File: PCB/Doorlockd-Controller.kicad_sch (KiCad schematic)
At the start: 58 parts, among them J10 Power Out 1, J11 Audio out, J12 GPIO 3, J13 Debug UART, J14 GPIO 4, J15 Power Out 2, J16 to extra screw conn., J18 GPIO only MilkV 1.8V, J19 3V 5V Vin, J20 3V 5V Vin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

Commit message: Added kibot workflow for automatic versioning
see https://github.com/matthijskooijman/PCB-workflows
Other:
- title: Doorlockd - BBB PCB -> Doorlockd-Controller (Rock pi-S/Milk-V duo S)
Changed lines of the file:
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@@
 	(paper "A4")
 	(title_block
-		(title "Doorlockd - BBB PCB")
-		(date "2019-06-11")
-		(rev "v0.02")
+		(title "Doorlockd-Controller (Rock pi-S/Milk-V duo S)")
+		(date "2025-06-17")
+		(rev "v2.0")
 		(comment 1 "author: Diederik Hamelink")
 		(comment 2 "CC BY 4.0")
+		(comment 3 "github.com/doorlockd")
 		(comment 4 "de WAR")
 	)
@@
 			"AAcAAAAHAAAABwAAAAcAAAAHAAAABwAAAAcAAAAHAAAABwAAAAcAAAAHAAAABwAAAAcAAAAHAAAA"
 			"BwAAAAcAAAAHAAAABwAAAAcAAAAHAAAABwAAAAcAAAAHAAAABwAAAAcAAAAHAAAABwAAAAcAAAAH"
-			"AAAABwAAAA=="
+			"AAAABwAAAAABAAAA8M3TJgEAAAAIBwAAAQAAAJDN0yYBAAAAEQAAAAEAAABgy9MmAQAAAODN0yYB"
+			"AAAAAAAAAAAAAAD/AQAAFgAAAP8BAABFAAAAGAAAAAEAAACwtbUHAQAAAAEAAAABAAAATQcAABMA"
+			"AAD/AQAAFgAAAP8BAAAgAAAATQQAAAEAAABAztMmAQAAAAkHAAABAAAAQMvTJgEAAABLBAAAIgAA"
+			"AEDO0yYBAAAACQcAAAEAAACgztMmAQAAADgEAAABAAAAQM7TJgEAAAAJBwAAIgAAAMDO0yYBAAAA"
+			"NwQAAAEAAABAztMmAQAAAAkHAAAAAAAA4M7TJgEAAAA2BAAAFwAAAEDO0yYBAAAACQcAAAEAAAAA"
+			"z9MmAQAAACoEAAABAAAAQM7TJgEAAAAJBwAAAQAAACDP0yYBAAAADwAAAAEAAABAztMmAQAAAAAA"
+			"AAAAAAAAYSIAAAEAAABIz9MmAQAAADcEAAABAAAAyM7TJgEAAAD/AQAAEAAAAP8BAABFAAAA8gMA"
+			"ACcAAABgz9MmAQAAAAkHAAABAAAAYMrTJgEAAAABAAAAAAAAAGDP0yYBAAAAcwQAADUAAAAAAAAA"
+			"AAAAAAoHAAABAAAAAAAAAAAAAABsBAAAAQAAAAAAAAAAAAAA/wAAAAEBAAAAgrwmAQAAAPAPUwAA"
+			"YAAAwA9TAABgAACAEFMAAGAAAAARUwAAYAAAABJTAABgAAAAAAAAAAAAAAAAAAAAAAAAAAAAAAAA"
+			"AAAAAAAAAAAAAAAAAAAAAAAAAAAAAAAAAAAAAAAAAAAAAAAAAAAAYAAAAAAAAAAAAAAAAAAAAAAA"
+			"AAAAAAAAAAAAAgAAAAAAAAAAAAAAAAAAAAAIbQYAYAAA4CvJAwBgAAAjAAAAAAAAACgAAAAAAACA"
+			"gB9TAABgAABAIFMAAGAAAAAhUwAAYAAAwCFTAABgAACAIlMAAGAAAEAjUwAAYAAAACRTAABgAADA"
+			"JFMAAGAAAIAlUwAAYAAAQCZTAABgAAAAJ1MAAGAAAPAzkWMBAAAAIDaRYwEAAABQOJFjAQAAAIA6"
+			"kWMBAAAAsDyRYwEAAADgPpFjAQAAABBBkWMBAAAAQEORYwEAAABwRZFjAQAAAKBHkWMBAAAA0EmR"
+			"YwEAAADAJ1MAAGAAAIAoUwAAYAAAQClTAABgAAAAKlMAAGAAAMAqUwAAYAAAgCtTAABgAABALFMA"
+			"AGAAAAAtUwAAYAAAwC1TAABgAACALlMAAGAAAEAvUwAAYAAAADBTAABgAADAMFMAAGAAAIAxUwAA"
+			"YAAAQDJTAABgAAAAM1MAAGAAAMAzUwAAYAAAgDRTAABgAABANVMAAGAAAAA2UwAAYAAAwDZTAABg"
+			"AACAN1MAAA=="
 		)
 	)

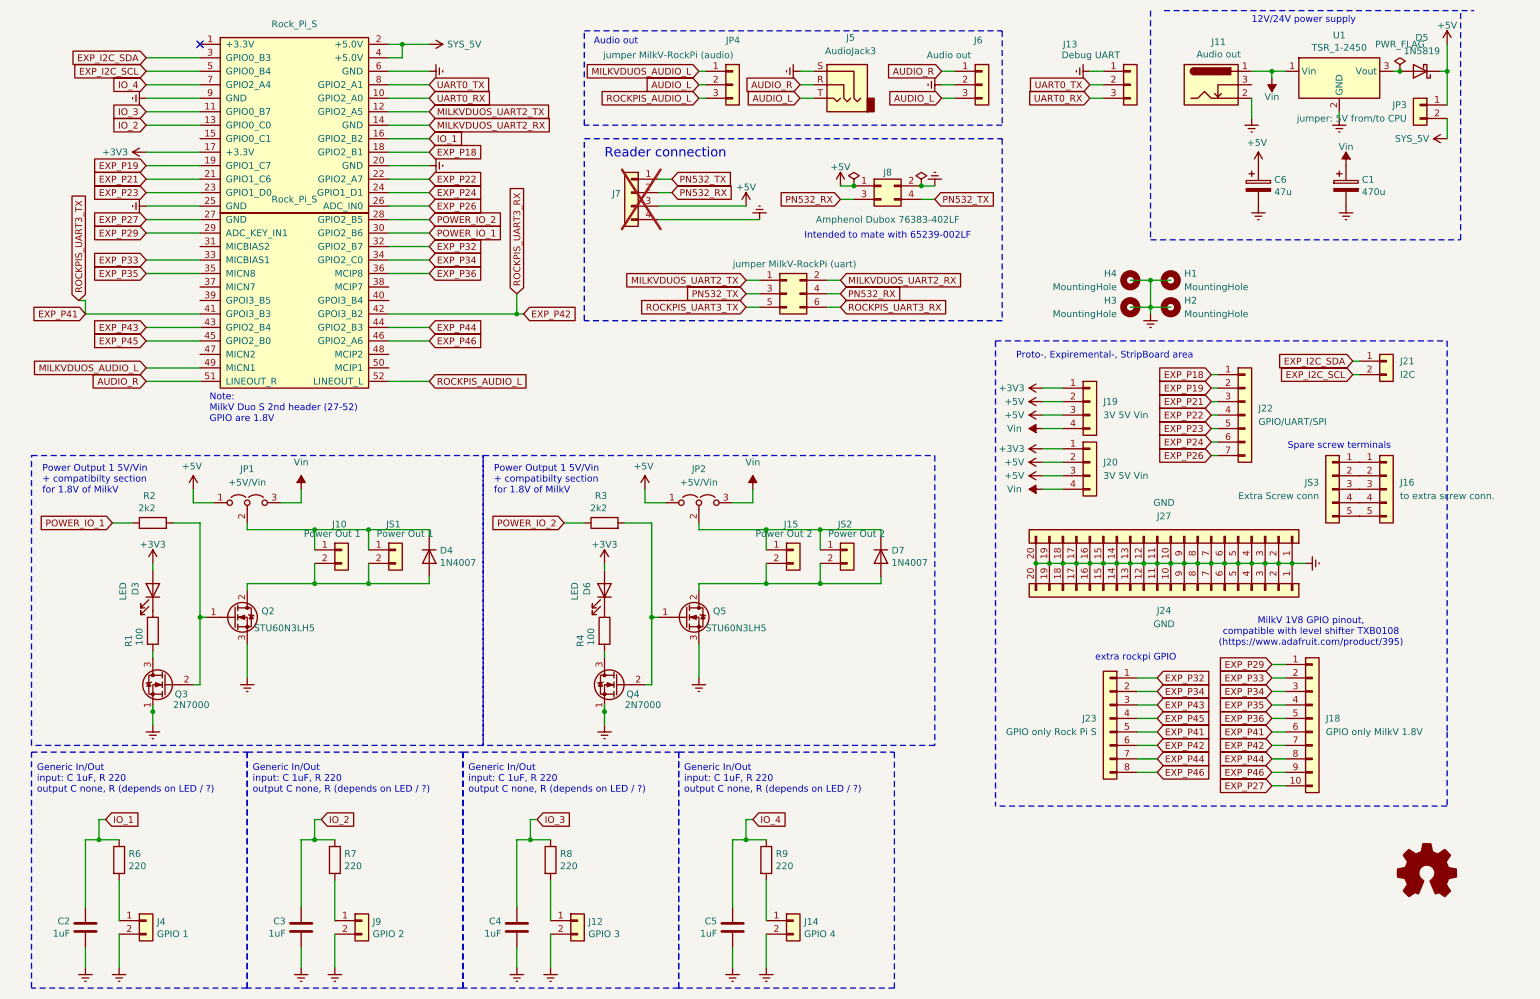
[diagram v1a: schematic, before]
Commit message: Fixed various ERC rule errors and warnings
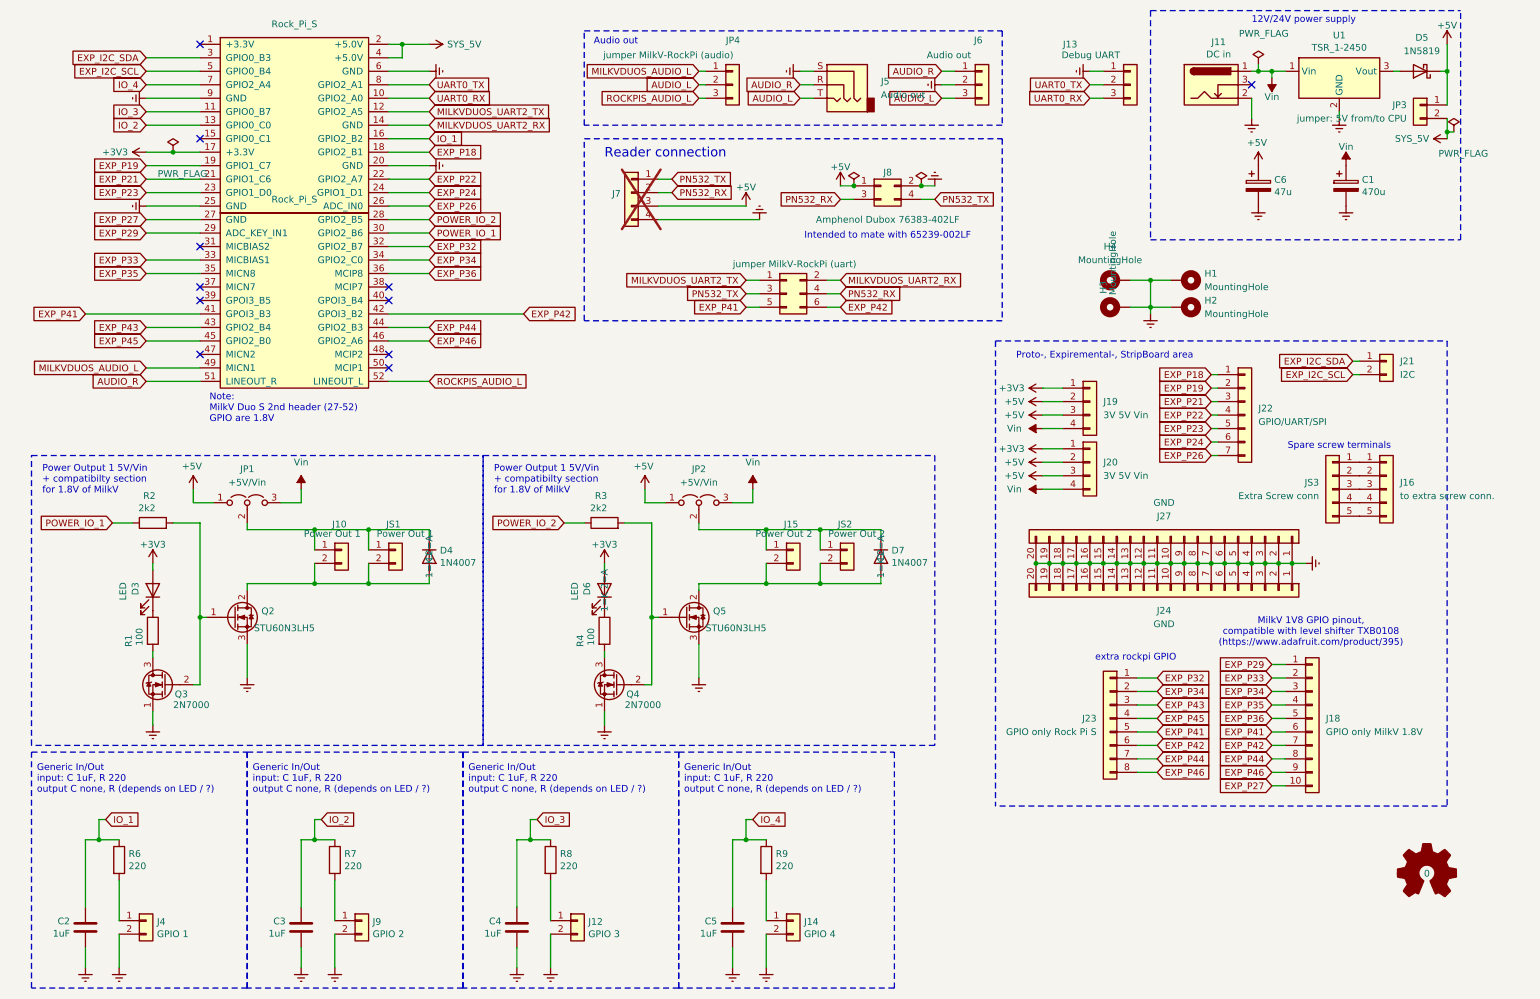
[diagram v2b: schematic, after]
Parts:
- D4, D7: footprint Diode_THT:D_DO-41_SOD81_P7.62mm_Horizontal -> Diode_THT:D_DO-41_SOD81_P10.16mm_Horizontal
- H1, H2, H3, H4: symbol Mechanical:MountingHole -> Mechanical:MountingHole_Pad
- J11: value Audio out -> DC in
- J5: value AudioJack3 -> Audio out
- Q2, Q5: symbol Device:Q_NMOS_GDS -> Transistor_FET:Q_NMOS_GDS
- Q3, Q4: footprint Package_TO_SOT_THT:TO-92_Wide -> Package_TO_SOT_THT:TO-92_Inline
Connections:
- net Earth: now also H1.1, H2.1, H3.1, H4.1
- no-connect marks 1 -> 11

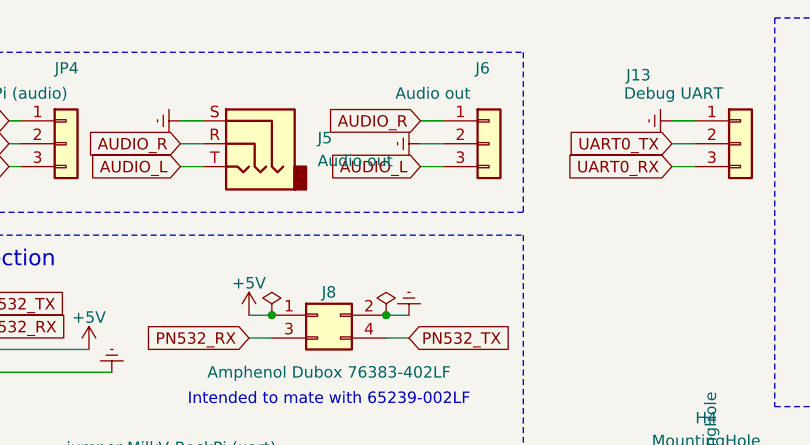
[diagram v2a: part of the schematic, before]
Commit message: Note audio jack actually to be used
The 1503 07 for which we used a footprint is no longer available, but
the 1503 30 should be pin compatible.
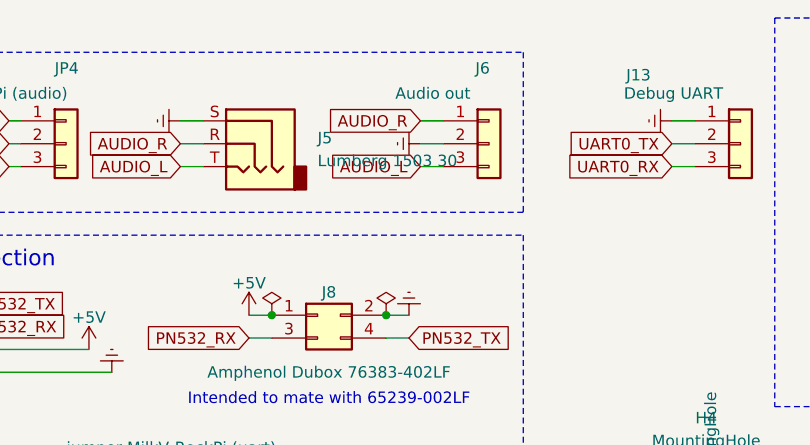
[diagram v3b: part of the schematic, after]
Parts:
- J5: value Audio out -> Lumberg 1503 30; Note (none) -> Lumberg 1503 30 and 07 are pin-compatible
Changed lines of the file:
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@@
 			)
 		)
-		(property "Value" "Audio out"
+		(property "Value" "Lumberg 1503 30"
 			(at 172.72 28.5749 0)
 			(effects
@@
 			(at 165.1 26.67 0)
 			(effects
+				(font
+					(size 1.27 1.27)
+				)
+				(hide yes)
+			)
+		)
+		(property "Note" "Lumberg 1503 30 and 07 are pin-compatible"
+			(at 165.1 26.67 0)
+			(effects

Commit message: Update footprints in schematic (from PCB)
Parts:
- D4, D7: footprint Diode_THT:D_DO-41_SOD81_P10.16mm_Horizontal -> Diode_THT:D_DO-41_SOD81_P7.62mm_Horizontal
- Q3, Q4: footprint Package_TO_SOT_THT:TO-92_Inline -> Package_TO_SOT_THT:TO-92_Wide
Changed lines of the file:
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@@
 			)
 		)
-		(property "Footprint" "Package_TO_SOT_THT:TO-92_Inline"
+		(property "Footprint" "Package_TO_SOT_THT:TO-92_Wide"
 			(at 118.11 141.605 0)
 			(effects
@@
 			)
 		)
-		(property "Footprint" "Package_TO_SOT_THT:TO-92_Inline"
+		(property "Footprint" "Package_TO_SOT_THT:TO-92_Wide"
 			(at 33.02 141.605 0)
 			(effects
@@
 			)
 		)
-		(property "Footprint" "Diode_THT:D_DO-41_SOD81_P10.16mm_Horizontal"
+		(property "Footprint" "Diode_THT:D_DO-41_SOD81_P7.62mm_Horizontal"
 			(at 168.275 115.57 0)
 			(effects
@@
 			)
 		)
-		(property "Footprint" "Diode_THT:D_DO-41_SOD81_P10.16mm_Horizontal"
+		(property "Footprint" "Diode_THT:D_DO-41_SOD81_P7.62mm_Horizontal"
 			(at 83.185 115.57 0)
 			(effects

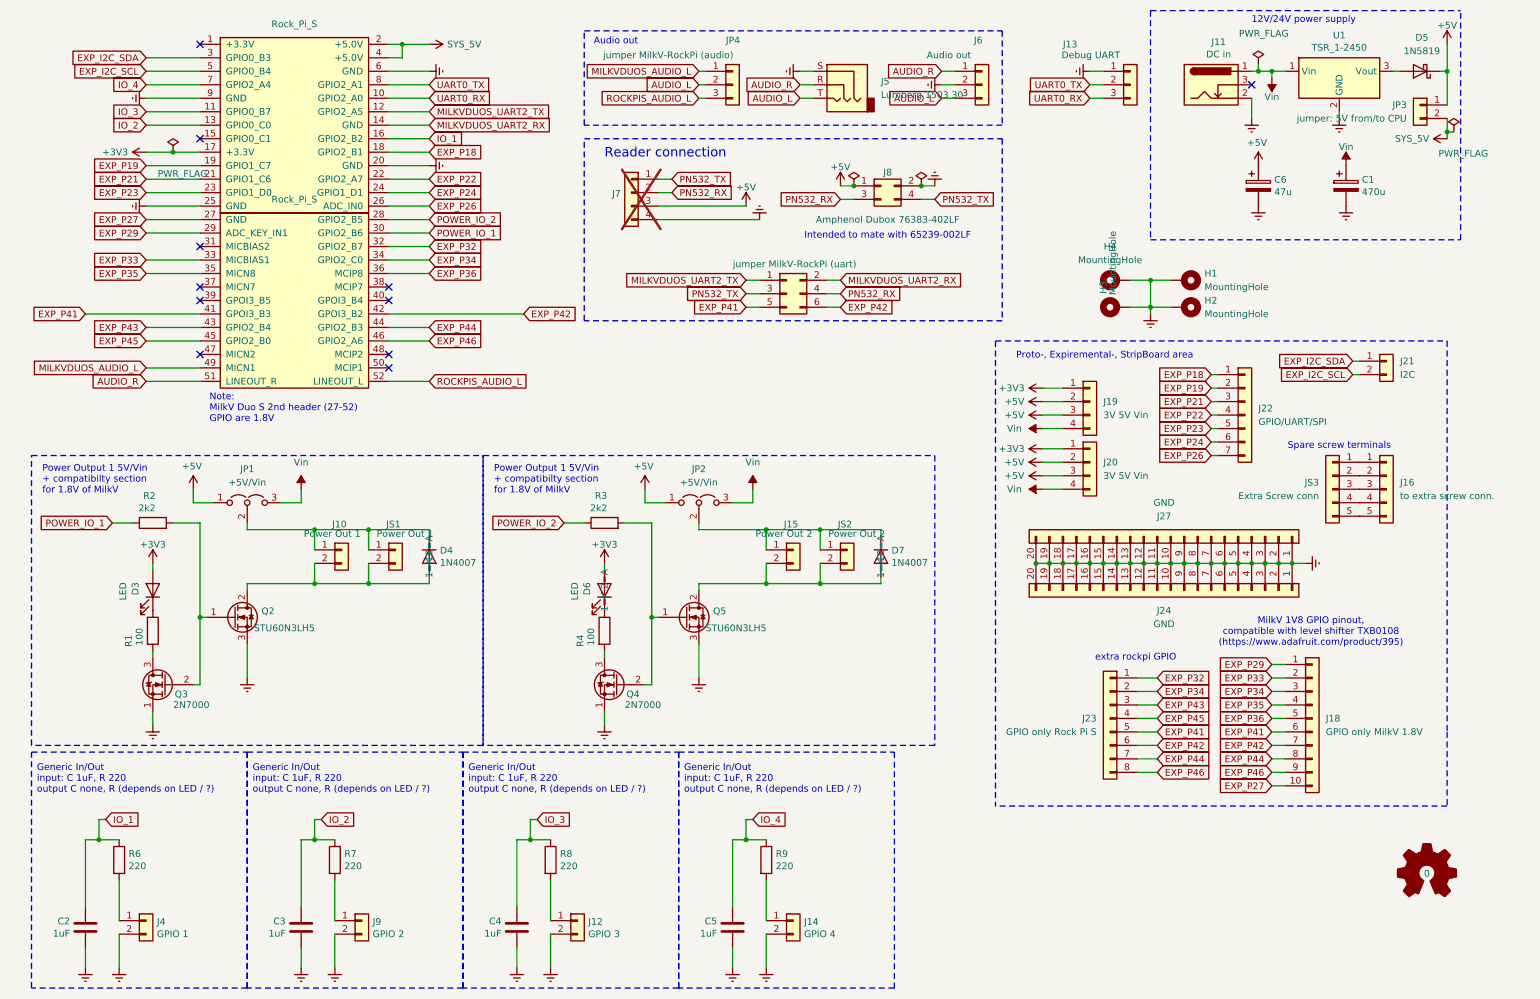
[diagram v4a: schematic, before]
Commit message: Fixed correct pins for ROCKPIS_UART3_RX/TX connecting PN532 Reader
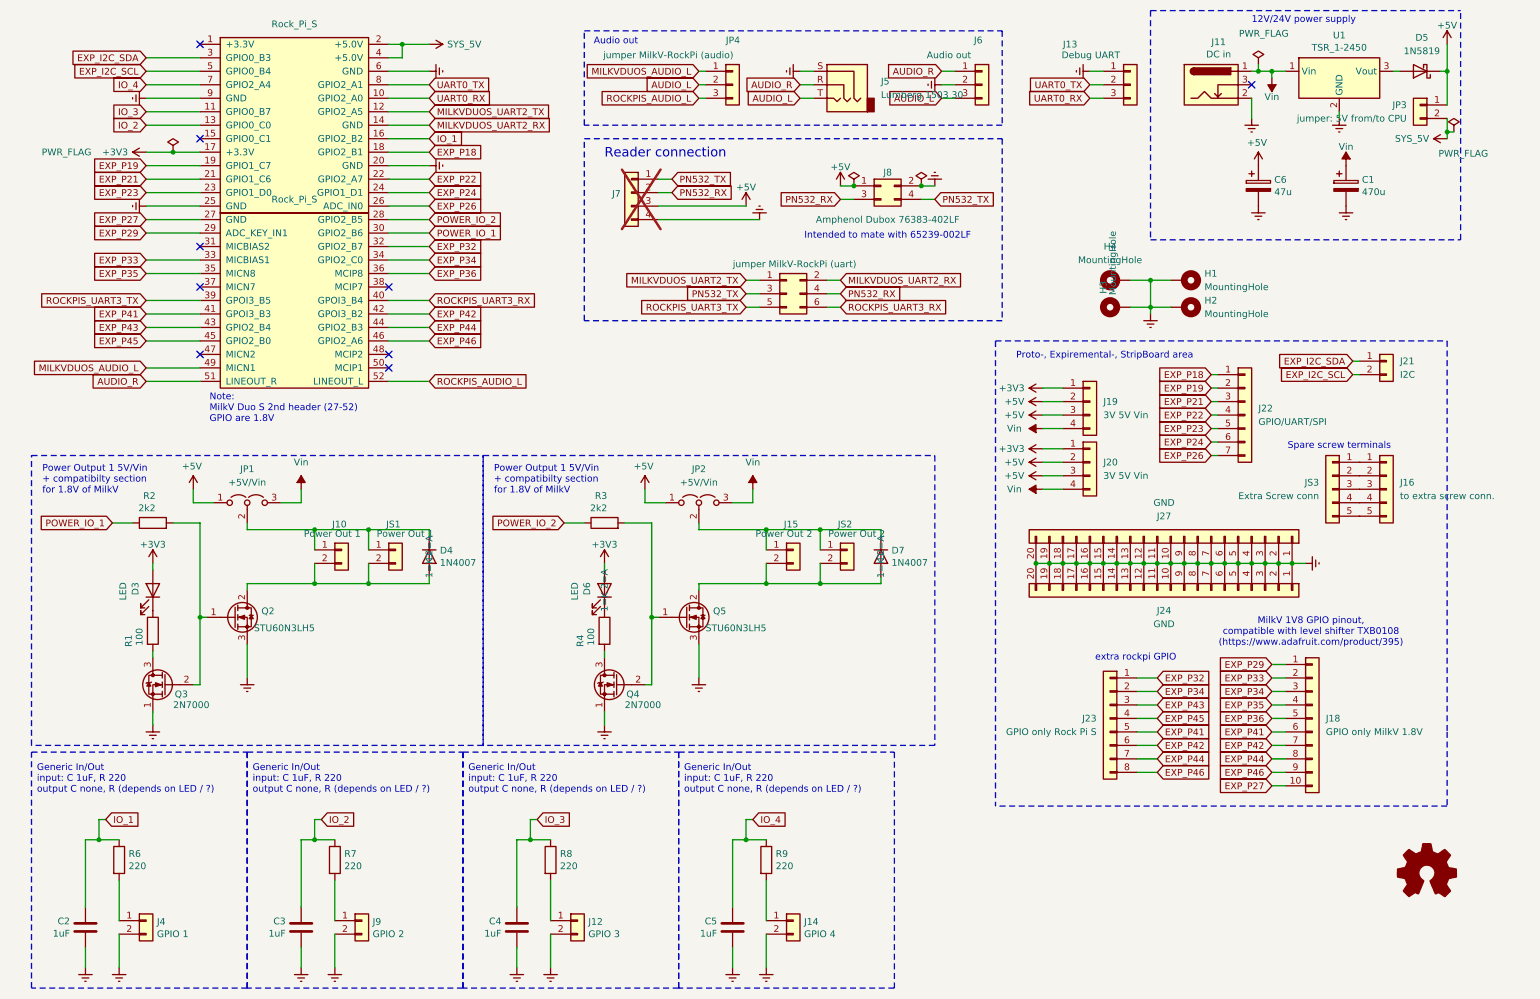
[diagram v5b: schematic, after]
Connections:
- net EXP_P41: no longer JP5.5 (Pin_5)
- net EXP_P42: no longer JP5.6 (Pin_6)
- net ROCKPIS_UART3_TX: now reaches U2.39 (GPOI3_B5)
- net ROCKPIS_UART3_TX: now also JP5.5 (Pin_5)
- net ROCKPIS_UART3_RX: now reaches U2.40 (GPOI3_B4)
- net ROCKPIS_UART3_RX: now also JP5.6 (Pin_6)
- no-connect marks 11 -> 9
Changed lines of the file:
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@@
 	)
 	(no_connect
-		(at 44.45 67.31)
-	)
-	(no_connect
 		(at 44.45 36.83)
 	)
@@
 	)
 	(no_connect
-		(at 80.01 67.31)
-	)
-	(no_connect
 		(at 44.45 57.15)
 	)
@@
 	(wire
 		(pts
+			(xy 80.01 67.31) (xy 87.63 67.31)
+		)
+		(stroke
+			(width 0)
+			(type default)
+		)
+	)
+	(wire
+		(pts
 			(xy 63.5 181.61) (xy 63.5 168.91)
 		)
@@
 	(wire
 		(pts
-			(xy 80.01 69.85) (xy 105.41 69.85)
+			(xy 80.01 69.85) (xy 87.63 69.85)
 		)
 		(stroke
@@
 	(wire
 		(pts
-			(xy 22.86 69.85) (xy 44.45 69.85)
+			(xy 34.29 69.85) (xy 44.45 69.85)
 		)
 		(stroke
@@
 	(wire
 		(pts
+			(xy 34.29 67.31) (xy 44.45 67.31)
+		)
+		(stroke
+			(width 0)
+			(type default)
+		)
+	)
+	(wire
+		(pts
 			(xy 76.2 120.65) (xy 87.63 120.65)
 		)
@@
 		)
 	)
-	(global_label "EXP_P41"
+	(global_label "ROCKPIS_UART3_TX"
 		(shape input)
 		(at 147.32 68.58 180)
@@
 		)
 		(property "Intersheetrefs" "${INTERSHEET_REFS}"
-			(at 136.7039 68.58 0)
+			(at 126.7857 68.58 0)
 			(effects
 				(font
@@
 	(global_label "EXP_P41"
 		(shape input)
-		(at 22.86 69.85 180)
+		(at 34.29 69.85 180)
 		(fields_autoplaced yes)
 		(effects
@@
 		)
 		(property "Intersheetrefs" "${INTERSHEET_REFS}"
-			(at 12.2439 69.85 0)
+			(at 23.6739 69.85 0)
 			(effects
 				(font
@@
 		)
 	)
-	(global_label "EXP_P42"
+	(global_label "ROCKPIS_UART3_RX"
 		(shape input)
 		(at 165.1 68.58 0)
@@
 		)
 		(property "Intersheetrefs" "${INTERSHEET_REFS}"
-			(at 175.7161 68.58 0)
+			(at 185.9367 68.58 0)
 			(effects
 				(font
@@
 	(global_label "EXP_P42"
 		(shape input)
-		(at 105.41 69.85 0)
+		(at 87.63 69.85 0)
 		(fields_autoplaced yes)
 		(effects
@@
 		)
 		(property "Intersheetrefs" "${INTERSHEET_REFS}"
-			(at 116.0261 69.85 0)
+			(at 98.2461 69.85 0)
 			(effects
 				(font
@@
 		)
 	)
+	(global_label "ROCKPIS_UART3_RX"
+		(shape input)
+		(at 87.63 67.31 0)
+		(fields_autoplaced yes)
+		(effects
+			(font
+				(size 1.27 1.27)
+			)
+			(justify left)
+		)
+		(property "Intersheetrefs" "${INTERSHEET_REFS}"
+			(at 108.4667 67.31 0)
+			(effects
+				(font
+					(size 1.27 1.27)
+				)
+				(justify left)
+				(hide yes)
+			)
+		)
+	)
 	(global_label "IO_1"
 		(shape input)
@@
 		)
 	)
+	(global_label "ROCKPIS_UART3_TX"
+		(shape input)
+		(at 34.29 67.31 180)
+		(fields_autoplaced yes)
+		(effects
+			(font
+				(size 1.27 1.27)
+			)
+			(justify right)
+		)
+		(property "Intersheetrefs" "${INTERSHEET_REFS}"
+			(at 13.7557 67.31 0)
+			(effects
+				(font
+					(size 1.27 1.27)
+				)
+				(justify right)
+				(hide yes)
+			)
+		)
+	)
 	(global_label "EXP_P41"
 		(shape input)
@@
 		(at 275.59 175.26 0)
 		(unit 1)
-		(exclude_from_sim no)
+		(exclude_from_sim yes)
 		(in_bom yes)
 		(on_board yes)
@@
 			)
 		)
-		(property "Sim.Enable" "0"
-			(at 275.59 175.26 0)
-			(effects
-				(font
-					(size 1.27 1.27)
-				)
-			)
-		)
 		(instances
 			(project ""
@@
 		)
 		(property "Value" "PWR_FLAG"
-			(at 41.148 43.434 0)
+			(at 19.304 39.37 0)
 			(effects
 				(font

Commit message: Fixed Pin 15 and updated the spreadsheet MILKVDUOS_UART2_RX was connected to the wrong pin14 -> pin15
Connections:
- net Earth: now also U2.14 (GND)
- net MILKVDUOS_UART2_RX: now also U2.15 (GPIO0_C1); no longer U2.14 (GND)
- no-connect marks 9 -> 8
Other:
- moved on the sheet: C1, C6, D5, H1, H2, H3, H4, J11, J13, J16, J5, J6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
